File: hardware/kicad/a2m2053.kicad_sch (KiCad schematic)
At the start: 0 parts

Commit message: feat(pcb): frame-ground mounting holes H1/H2
Both M3 holes become plated footprints on net FG, placed from the
schematic. H2 uses the stock MountingHole_3.2mm_M3_Pad_Via. H1 sits
3.1 mm from the board edge, so it gets a project footprint with a
5.2 mm pad to keep 0.5 mm copper-to-edge. DRC: 0 violations; the
only unconnected item is FG between H1 and H2, not routed yet.

The outline script no longer draws hole circles; it positions H1/H2,
with a warning that footprint moves through the API crashed KiCad.

Co-Authored-By: Claude Opus 5.5 <noreply@anthropic.com>
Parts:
- added H1: M3 frame ground, a2m2053:MountingHole_3.2mm_M3_Pad_5.2mm, symbol Mechanical:MountingHole_Pad
- added H2: M3 frame ground, MountingHole:MountingHole_3.2mm_M3_Pad_Via, symbol Mechanical:MountingHole_Pad
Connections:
- new net FG: H1.1, H2.1
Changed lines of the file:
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@@
 	(generator_version "9.0")
 	(paper "A4")
+	(symbol
+		(lib_id "Mechanical:MountingHole_Pad")
+		(at 101.6 50.8 0)
+		(unit 1)
+		(exclude_from_sim no)
+		(in_bom no)
+		(on_board yes)
+		(dnp no)
+		(property "Reference" "H1"
+			(at 104.14 46.989999999999995 0)
+			(effects (font (size 1.27 1.27)) (justify left))
+		)
+		(property "Value" "M3 frame ground"
+			(at 104.14 49.529999999999994 0)
+			(effects (font (size 1.27 1.27)) (justify left))
+		)
+		(property "Footprint" "a2m2053:MountingHole_3.2mm_M3_Pad_5.2mm"
+			(at 101.6 50.8 0)
+			(effects (font (size 1.27 1.27)) (hide yes))
+		)
+		(property "Datasheet" "~"
+			(at 101.6 50.8 0)
+			(effects (font (size 1.27 1.27)) (hide yes))
+		)
+		(property "Description" "Mounting hole to the chassis, frame ground"
+			(at 101.6 50.8 0)
+			(effects (font (size 1.27 1.27)) (hide yes))
+		)
+		(pin "1"
+		)
+		(instances
+			(project "a2m2053"
+				(path "/a667a28b-9b2a-40ce-b2bb-952e798c6355"
+					(reference "H1")
+					(unit 1)
+				)
+			)
+		)
+	)
+	(global_label "FG"
+		(shape passive)
+		(at 101.6 53.34 270)
+		(effects (font (size 1.27 1.27)) (justify right))
+		(property "Intersheetrefs" "${INTERSHEET_REFS}"
+			(at 0 0 0)
+			(effects (font (size 1.27 1.27)) (hide yes))
+		)
+	)
+	(symbol
+		(lib_id "Mechanical:MountingHole_Pad")
+		(at 121.92 50.8 0)
+		(unit 1)
+		(exclude_from_sim no)
+		(in_bom no)
+		(on_board yes)
+		(dnp no)
+		(property "Reference" "H2"
+			(at 124.46000000000001 46.989999999999995 0)
+			(effects (font (size 1.27 1.27)) (justify left))
+		)
+		(property "Value" "M3 frame ground"
+			(at 124.46000000000001 49.529999999999994 0)
+			(effects (font (size 1.27 1.27)) (justify left))
+		)
+		(property "Footprint" "MountingHole:MountingHole_3.2mm_M3_Pad_Via"
+			(at 121.92 50.8 0)
+			(effects (font (size 1.27 1.27)) (hide yes))
+		)
+		(property "Datasheet" "~"
+			(at 121.92 50.8 0)
+			(effects (font (size 1.27 1.27)) (hide yes))
+		)
+		(property "Description" "Mounting hole to the chassis, frame ground"
+			(at 121.92 50.8 0)
+			(effects (font (size 1.27 1.27)) (hide yes))
+		)
+		(pin "1"
+		)
+		(instances
+			(project "a2m2053"
+				(path "/a667a28b-9b2a-40ce-b2bb-952e798c6355"
+					(reference "H2")
+					(unit 1)
+				)
+			)
+		)
+	)
+	(global_label "FG"
+		(shape passive)
+		(at 121.92 53.34 270)
+		(effects (font (size 1.27 1.27)) (justify right))
+		(property "Intersheetrefs" "${INTERSHEET_REFS}"
+			(at 0 0 0)
+			(effects (font (size 1.27 1.27)) (hide yes))
+		)
+	)
 	(sheet_instances
 		(path "/"

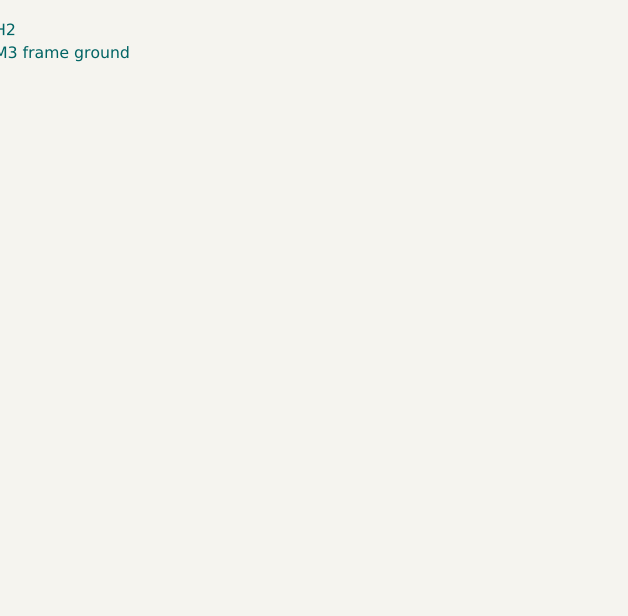
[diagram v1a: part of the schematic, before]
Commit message: feat(pcb): rear DB-19 J1 placed and fit-checked, step depths corrected
- J1: female right-angle DB-19 (daisy-chain port), 38.8 mm board-lock
  footprint on FG, face at the 94 mm top edge. Placement checked with a
  3D print holding the real connector on the IF-83 mounting points and
  in the case opening.
- Outline steps are 12 mm deep on the left and 6 mm on the right, checked
  on the IF-83. kicad_outline.py gains --outline-only.
- Photos of the fit check, EXIF stripped.

Co-Authored-By: Claude Opus 5.5 <noreply@anthropic.com>
Claude-Session: https://claude.ai/code/session_019cEGosXJSu4icn9o4uaZwB
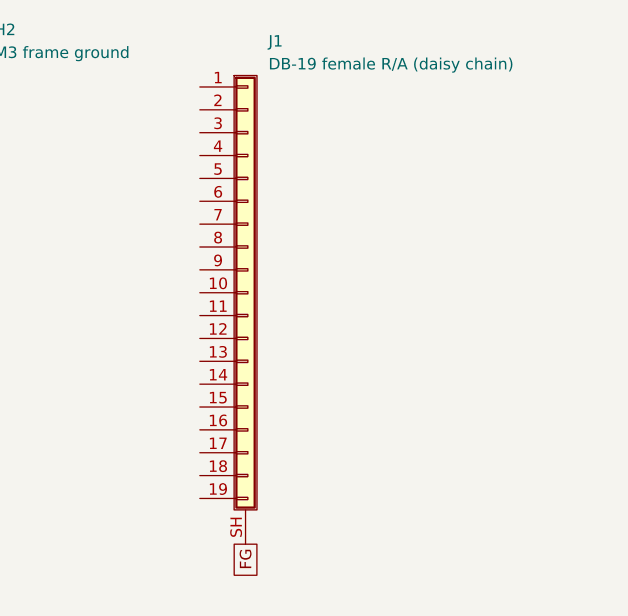
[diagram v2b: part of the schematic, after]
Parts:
- added J1: DB-19 female R/A (daisy chain), a2m2053:DSUB-19_Female_Horizontal_P2.77x2.84mm_MountingHoles38.8mm, symbol Connector_Generic_Shielded:Conn_01x19_Shielded
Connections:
- net FG: now also J1.SH (Shield)
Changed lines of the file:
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@@
+		)
+	)
+	(symbol
+		(lib_id "Connector_Generic_Shielded:Conn_01x19_Shielded")
+		(at 152.4 76.2 0)
+		(unit 1)
+		(exclude_from_sim no)
+		(in_bom yes)
+		(on_board yes)
+		(dnp no)
+		(property "Reference" "J1"
+			(at 154.94 48.260000000000005 0)
+			(effects (font (size 1.27 1.27)) (justify left))
+		)
+		(property "Value" "DB-19 female R/A (daisy chain)"
+			(at 154.94 50.800000000000004 0)
+			(effects (font (size 1.27 1.27)) (justify left))
+		)
+		(property "Footprint" "a2m2053:DSUB-19_Female_Horizontal_P2.77x2.84mm_MountingHoles38.8mm"
+			(at 152.4 76.2 0)
+			(effects (font (size 1.27 1.27)) (hide yes))
+		)
+		(property "Datasheet" "~"
+			(at 152.4 76.2 0)
+			(effects (font (size 1.27 1.27)) (hide yes))
+		)
+		(property "Description" "Rear DB-19 daisy-chain port, female right angle; shell board locks on FG"
+			(at 152.4 76.2 0)
+			(effects (font (size 1.27 1.27)) (hide yes))
+		)
+		(pin "1"
+		)
+		(pin "2"
+		)
+		(pin "3"
+		)
+		(pin "4"
+		)
+		(pin "5"
+		)
+		(pin "6"
+		)
+		(pin "7"
+		)
+		(pin "8"
+		)
+		(pin "9"
+		)
+		(pin "10"
+		)
+		(pin "11"
+		)
+		(pin "12"
+		)
+		(pin "13"
+		)
+		(pin "14"
+		)
+		(pin "15"
+		)
+		(pin "16"
+		)
+		(pin "17"
+		)
+		(pin "18"
+		)
+		(pin "19"
+		)
+		(pin "SH"
+		)
+		(instances
+			(project "a2m2053"
+				(path "/a667a28b-9b2a-40ce-b2bb-952e798c6355"
+					(reference "J1")
+					(unit 1)
+				)
+			)
+		)
+	)
+	(global_label "FG"
+		(shape passive)
+		(at 152.4 104.14 270)
+		(effects (font (size 1.27 1.27)) (justify right))
+		(property "Intersheetrefs" "${INTERSHEET_REFS}"
+			(at 0 0 0)
+			(effects (font (size 1.27 1.27)) (hide yes))
 		)
 	)

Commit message: feat(pcb): schematic wired, parts placed, board autorouted
Schematic: Pico 2 (A1), five SN74LVC8T245 (U1-U5) with one 100 nF per
rail, pull-ups/pull-downs, D1 Schottky to VSYS, 4.7 uF 50 V bulk caps,
J2 (CN104) and J3 (CN102) 2x10 headers, J4 eject and J5 LED headers.

Board: all parts placed inside the IF-83 outline, Pico USB at the bottom
edge. Netclasses Power (+5V, +12V, -12V: 1.0 mm), Rail (+3V3, VSYS:
0.5 mm). GND pour on B.Cu, +5V pour on F.Cu. Tracks from Freerouting
2.1.0 (r5, 80 vias); -12V J1.5 to J3.9 routed by hand at 0.25 mm.

Routing scratch (DSN/SES runs, DRC dumps, helper scripts) lives in
hardware/kicad/scratch/, git-ignored except for its .gitkeep.

DRC: 0 unconnected. Open: EJECT via 0.42 mm from the left edge, starved
thermals on J1.4 and J3.5, silkscreen warnings, A1 library mismatch.

Co-Authored-By: Claude Opus 5.5 <noreply@anthropic.com>
Claude-Session: https://claude.ai/code/session_019cEGosXJSu4icn9o4uaZwB
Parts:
- added A1: Pico 2, Module:RaspberryPi_Pico_SMD_HandSolder, symbol MCU_Module:RaspberryPi_Pico
- added C1, C10, C2, C3, C4, C5, C6, C7, C8, C9: 100nF, Capacitor_SMD:C_0805_2012Metric, symbol Device:C
- added C11, C12, C13: 4.7uF 50V, Capacitor_THT:CP_Radial_D5.0mm_P2.00mm, symbol Device:C_Polarized
- added D1: STPS2L40AF, Diode_SMD:D_SMA, symbol Device:D_Schottky_Small
- added J2: CN104 mechanism, Connector_IDC:IDC-Header_2x10_P2.54mm_Vertical, symbol Connector_Generic:Conn_02x10_Odd_Even
- added J3: CN102 host (FROM HOST), Connector_IDC:IDC-Header_2x10_P2.54mm_Vertical, symbol Connector_Generic:Conn_02x10_Odd_Even
- added J4: Eject button, Connector_PinHeader_2.54mm:PinHeader_1x03_P2.54mm_Vertical, symbol Connector_Generic:Conn_01x03
- added J5: In-use LED, Connector_PinHeader_2.54mm:PinHeader_1x02_P2.54mm_Vertical, symbol Connector_Generic:Conn_01x02
- added R1, R11, R12, R13, R14, R15, R2, R3, R4, R5, R6, R7, R8, R9: 10k, Resistor_SMD:R_1206_3216Metric, symbol Device:R
- added R10: 100k, Resistor_SMD:R_1206_3216Metric, symbol Device:R
- added R16: 2k, Resistor_SMD:R_1206_3216Metric, symbol Device:R
- added R17: 330, Resistor_SMD:R_1206_3216Metric, symbol Device:R
- added U1, U2, U3, U4, U5: SN74LVC8T245DWR, Package_SO:SOIC-24W_7.5x15.4mm_P1.27mm, symbol Logic_LevelTranslator:SN74LVC8T245
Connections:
- net GND: now reaches J1.1 (Pin_1)
- net GND: now also J1.2 (Pin_2), J1.3 (Pin_3), J1.4 (Pin_4), A1.13 (GND), A1.18 (GND), A1.23 (GND), A1.28 (GND), A1.3 (GND), A1.33 (AGND), A1.38 (GND), A1.8 (GND), C1.2, C10.2, C11.2, C12.2, C13.2, C2.2, C3.2, C4.2, C5.2, C6.2, C7.2, C8.2, C9.2, J2.1 (Pin_1), J2.3 (Pin_3), J2.5 (Pin_5), J2.7 (Pin_7), J3.1 (Pin_1), J3.12 (Pin_12), J3.3 (Pin_3), J3.5 (Pin_5), J3.7 (Pin_7), J4.1 (Pin_1), J4.3 (Pin_3), J5.2 (Pin_2), R10.2, R14.2, R4.2, R5.2, R6.2, R7.2, U1.11 (GND), U1.12 (GND), U1.13 (GND), U1.2 (DIR), U1.22 (~{OE}), U2.11 (GND), U2.12 (GND), U2.13 (GND), U3.10 (A8), U3.11 (GND), U3.12 (GND), U3.13 (GND), U3.5 (A3), U3.6 (A4), U3.7 (A5), U3.8 (A6), U3.9 (A7), U4.10 (A8), U4.11 (GND), U4.12 (GND), U4.13 (GND), U4.6 (A4), U4.7 (A5), U4.8 (A6), U4.9 (A7), U5.11 (GND), U5.12 (GND), U5.13 (GND), U5.14 (B8), U5.15 (B7), U5.16 (B6), U5.17 (B5), U5.18 (B4), U5.19 (B3), U5.2 (DIR), U5.20 (B2), U5.22 (~{OE})
- net HOST_ACK: now reaches J1.10 (Pin_10)
- net HOST_ACK: now also J3.20 (Pin_20), R11.1, U3.20 (B2)
- net HOST_PH0: now reaches J1.11 (Pin_11)
- net HOST_PH0: now also J3.2 (Pin_2), R4.1, U1.21 (B1)
- net HOST_PH1: now reaches J1.12 (Pin_12)
- net HOST_PH1: now also J3.4 (Pin_4), R5.1, U1.20 (B2)
- net HOST_PH2: now reaches J1.13 (Pin_13)
- net HOST_PH2: now also J3.6 (Pin_6), R6.1, U1.19 (B3)
- net PH3_OUT: now reaches J1.14 (Pin_14)
- net PH3_OUT: now also R14.1, U4.21 (B1)
- net HOST_WRREQ: now reaches J1.15 (Pin_15)
- net HOST_WRREQ: now also J3.10 (Pin_10), R8.1, U1.17 (B5)
- net LASTONE: now reaches J1.16 (Pin_16)
- net LASTONE: now also R16.1, U5.21 (B1)
- net ENBL_OUT: now reaches J1.17 (Pin_17)
- net ENBL_OUT: now also R15.1, U4.20 (B2)
- net HOST_RD: now reaches J1.18 (Pin_18)
- net HOST_RD: now also J3.16 (Pin_16), U3.21 (B1)
- net HOST_WR: now reaches J1.19 (Pin_19)
- net HOST_WR: now also J3.18 (Pin_18), R10.1, U1.15 (B7)
- net -12V: now reaches J1.5 (Pin_5)
- net -12V: now also J3.9 (Pin_9)
- net +5V: now reaches J1.6 (Pin_6)
- net +5V: now also C10.1, C12.1, C2.1, C4.1, C6.1, C8.1, D1.2 (A), J2.11 (Pin_11), J2.20 (Pin_20), J3.11 (Pin_11), R1.2, R11.2, R15.2, R16.2, R2.2, R3.2, R8.2, R9.2, U1.23 (V_{CCB}), U1.24 (V_{CCB}), U2.23 (V_{CCB}), U2.24 (V_{CCB}), U3.23 (V_{CCB}), U3.24 (V_{CCB}), U4.23 (V_{CCB}), U4.24 (V_{CCB}), U5.23 (V_{CCB}), U5.24 (V_{CCB})
- net +12V: now reaches J1.7 (Pin_7)
- net +12V: now also J1.8 (Pin_8), C11.1, J2.13 (Pin_13), J2.15 (Pin_15), J2.17 (Pin_17), J2.19 (Pin_19), J3.13 (Pin_13), J3.15 (Pin_15)
- net HDSEL: now reaches J1.9 (Pin_9)
- net HDSEL: now also J3.17 (Pin_17)
- new net +3V3: A1.36 (3V3), C1.1, C13.1, C3.1, C5.1, C7.1, C9.1, R12.2, R13.2, U1.1 (V_{CCA}), U2.1 (V_{CCA}), U2.2 (DIR), U3.1 (V_{CCA}), U3.2 (DIR), U4.1 (V_{CCA}), U4.2 (DIR), U5.1 (V_{CCA})
- new net ACK_A: A1.12 (GPIO9), U3.4 (A2)
- new net CA0_A: A1.16 (GPIO12), U2.3 (A1)
- new net CA1_A: A1.17 (GPIO13), U2.4 (A2)
- new net CA2_A: A1.19 (GPIO14), U2.5 (A3)
- new net EJECT: A1.29 (GPIO22), J4.2 (Pin_2)
- new net ENBL_A: A1.22 (GPIO17), U2.8 (A6)
- new net ENBL_OUT_A: A1.32 (GPIO27_ADC1), U4.4 (A2)
- new net HOST_HSTEN: J3.14 (Pin_14), R9.1, U1.16 (B6)
- new net HOST_PH3: J3.8 (Pin_8), R7.1, U1.18 (B4)
- new net HOST_RD_A: A1.14 (GPIO10), U3.3 (A1)
- new net HSTEN_A: A1.10 (GPIO7), U1.8 (A6)
- new net LASTONE_A: A1.2 (GPIO1), U5.3 (A1)
- new net LED: J5.1 (Pin_1), R17.2
- new net LED_A: A1.31 (GPIO26_ADC0), U4.5 (A3)
- new net LED_B: R17.1, U4.19 (B3)
- new net LSTRB_A: A1.20 (GPIO15), U2.6 (A4)
- new net MECH_CA0: J2.2 (Pin_2), U2.21 (B1)
- new net MECH_CA1: J2.4 (Pin_4), U2.20 (B2)
- new net MECH_CA2: J2.6 (Pin_6), U2.19 (B3)
- new net MECH_ENBL: J2.14 (Pin_14), R2.1, U2.16 (B6)
- new net MECH_LSTRB: J2.8 (Pin_8), U2.18 (B4)
- new net MECH_RD: J2.16 (Pin_16), R1.1, U1.14 (B8)
- new net MECH_RD_A: A1.26 (GPIO20), U1.10 (A8)
- new net MECH_SEL: J2.12 (Pin_12), U2.17 (B5)
- new net MECH_WRTDATA: J2.18 (Pin_18), U2.14 (B8)
- new net MECH_WRTGATE: J2.10 (Pin_10), R3.1, U2.15 (B7)
- new net PH0_A: A1.4 (GPIO2), U1.3 (A1)
- new net PH1_A: A1.5 (GPIO3), U1.4 (A2)
- new net PH2_A: A1.6 (GPIO4), U1.5 (A3)
- new net PH3_A: A1.7 (GPIO5), U1.6 (A4)
- new net PH3_OUT_A: A1.1 (GPIO0), U4.3 (A1)
- new net SEL_A: A1.21 (GPIO16), U2.7 (A5)
- new net U2_OE: A1.27 (GPIO21), R13.1, U2.22 (~{OE}), U4.22 (~{OE})
- new net U3_OE: A1.15 (GPIO11), R12.1, U3.22 (~{OE})
- new net VSYS: A1.39 (VSYS), D1.1 (K)
- new net WRREQ_A: A1.9 (GPIO6), U1.7 (A5)
- new net WRTDATA_A: A1.25 (GPIO19), U2.10 (A8)
- new net WRTGATE_A: A1.24 (GPIO18), U2.9 (A7)
- new net WR_A: A1.11 (GPIO8), U1.9 (A7)
- no-connect marks 0 -> 25
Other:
- moved on the sheet: J1

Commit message: feat(pcb): place and route the controller board
Schematic: add R18 (10k LSTRB pull-down to GND, matches the rig) and
re-order 8T245 channels on U1, U2 and U5 so the fan-outs do not cross.
HANDOFF lists the eight prototype rewires.

PCB: place all parts, route host, rear, mechanism and Pico fan-outs,
+5V and GND pours, a +12V band under the mechanism power path, stitch
the Pico GND castellations and the host pull-up pour strips. DRC with
zone refill: 0 errors; one stray via to delete in pcbnew (noted in
HANDOFF).

Co-Authored-By: Claude Fable 5.1 <noreply@anthropic.com>
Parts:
- added R18: 10k, Resistor_SMD:R_1206_3216Metric, symbol Device:R
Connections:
- net CA0_A: now also U2.6 (A4); no longer U2.3 (A1)
- net CA1_A: now also U2.5 (A3); no longer U2.4 (A2)
- net CA2_A: now also U2.4 (A2); no longer U2.5 (A3)
- net GND: now also R18.2
- net HOST_HSTEN: now also U1.15 (B7); no longer U1.16 (B6)
- net HOST_WR: now also U1.14 (B8); no longer U1.15 (B7)
- net HSTEN_A: now also U1.9 (A7); no longer U1.8 (A6)
- net LASTONE: now also U1.16 (B6); no longer U5.21 (B1)
- net LASTONE_A: now also U1.8 (A6); no longer U5.3 (A1)
- net LSTRB_A: now also U2.3 (A1); no longer U2.6 (A4)
- net MECH_CA0: now also U2.18 (B4); no longer U2.21 (B1)
- net MECH_CA1: now also U2.19 (B3); no longer U2.20 (B2)
- net MECH_CA2: now also U2.20 (B2); no longer U2.19 (B3)
- net MECH_LSTRB: now also U2.21 (B1), R18.1; no longer U2.18 (B4)
- net MECH_RD: now also U5.21 (B1); no longer U1.14 (B8)
- net MECH_RD_A: now also U5.3 (A1); no longer U1.10 (A8)
- net WR_A: now also U1.10 (A8); no longer U1.9 (A7)

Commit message: feat(pcb): Byte Hamr logo and board text, FG merged into GND
Silkscreen: logo_sm footprint from Byte Hamr rev 2 (copied into the
project library), title, revision and ID block in the bottom-right
corner. Board named Disk Hamr.

Schematic: the three FG global labels on H1, H2 and the J1 shield become
GND power symbols; FG was a fit-test placeholder, frame ground is the
same return. PCB pads were already on GND. Schematic parity, DRC with
refill and ERC are clean apart from the pre-existing Pico AGND/GND pin
type error.

Co-Authored-By: Claude Fable 5.1 <noreply@anthropic.com>
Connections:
- net FG is gone; now on net GND: H1.1, H2.1, J1.SH (Shield)
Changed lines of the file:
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@@
 		)
 	)
-	(global_label "FG"
-		(shape passive)
-		(at 370.84 130.81 270)
-		(effects
-			(font
-				(size 1.27 1.27)
-			)
-			(justify right)
-		)
-		(property "Intersheetrefs" "${INTERSHEET_REFS}"
-			(at 370.84 130.81 0)
-			(hide yes)
-			(show_name no)
-			(do_not_autoplace no)
-			(effects
-				(font
-					(size 1.27 1.27)
-				)
-			)
-		)
-	)
-	(global_label "FG"
-		(shape passive)
-		(at 101.6 53.34 270)
-		(effects
-			(font
-				(size 1.27 1.27)
-			)
-			(justify right)
-		)
-		(property "Intersheetrefs" "${INTERSHEET_REFS}"
-			(at 101.6 57.5725 90)
-			(hide yes)
-			(show_name no)
-			(do_not_autoplace no)
-			(effects
-				(font
-					(size 1.27 1.27)
-				)
-				(justify right)
-			)
-		)
-	)
-	(global_label "FG"
-		(shape passive)
-		(at 121.92 53.34 270)
-		(effects
-			(font
-				(size 1.27 1.27)
-			)
-			(justify right)
-		)
-		(property "Intersheetrefs" "${INTERSHEET_REFS}"
-			(at 121.92 57.5725 90)
-			(hide yes)
-			(show_name no)
-			(do_not_autoplace no)
-			(effects
-				(font
-					(size 1.27 1.27)
-				)
-				(justify right)
-			)
-		)
-	)
 	(symbol
 		(lib_id "Connector_Generic:Conn_02x10_Odd_Even")
@@
 					(unit 1)
 				)
+			)
+		)
+	)
+	(symbol
+		(lib_id "power:GND")
+		(at 370.84 130.81 0)
+		(unit 1)
+		(in_bom yes)
+		(on_board yes)
+		(dnp no)
+		(property "Reference" "#PWR010"
+			(at 370.84 137.16 0)
+			(hide yes)
+			(effects
+				(font
+					(size 1.27 1.27)
+				)
+			)
+		)
+		(property "Value" "GND"
+			(at 370.84 134.62 0)
+			(effects
+				(font
+					(size 1.27 1.27)
+				)
+			)
+		)
+		(property "Footprint" ""
+			(at 370.84 130.81 0)
+			(hide yes)
+			(effects
+				(font
+					(size 1.27 1.27)
+				)
+			)
+		)
+		(property "Datasheet" ""
+			(at 370.84 130.81 0)
+			(hide yes)
+			(effects
+				(font
+					(size 1.27 1.27)
+				)
+			)
+		)
+		(property "Description" "Power symbol creates a global label with name \"GND\" , ground"
+			(at 370.84 130.81 0)
+			(hide yes)
+			(effects
+				(font
+					(size 1.27 1.27)
+				)
+			)
+		)
+		(instances
+			(project "a2m2053"
+				(path "/a667a28b-9b2a-40ce-b2bb-952e798c6355"
+					(reference "#PWR010")
+					(unit 1)
+				)
+			)
+		)
+	)
+	(symbol
+		(lib_id "power:GND")
+		(at 101.6 53.34 0)
+		(unit 1)
+		(in_bom yes)
+		(on_board yes)
+		(dnp no)
+		(property "Reference" "#PWR011"
+			(at 101.6 59.69 0)
+			(hide yes)
+			(effects
+				(font
+					(size 1.27 1.27)
+				)
+			)
+		)
+		(property "Value" "GND"
+			(at 101.6 57.15 0)
+			(effects
+				(font
+					(size 1.27 1.27)
+				)
+			)
+		)
+		(property "Footprint" ""
+			(at 101.6 53.34 0)
+			(hide yes)
+			(effects
+				(font
+					(size 1.27 1.27)
+				)
+			)
+		)
+		(property "Datasheet" ""
+			(at 101.6 53.34 0)
+			(hide yes)
+			(effects
+				(font
+					(size 1.27 1.27)
+				)
+			)
+		)
+		(property "Description" "Power symbol creates a global label with name \"GND\" , ground"
+			(at 101.6 53.34 0)
+			(hide yes)
+			(effects
+				(font
+					(size 1.27 1.27)
+				)
+			)
+		)
+		(instances
+			(project "a2m2053"
+				(path "/a667a28b-9b2a-40ce-b2bb-952e798c6355"
+					(reference "#PWR011")
+					(unit 1)
+				)
+			)
+		)
+	)
+	(symbol
+		(lib_id "power:GND")
+		(at 121.92 53.34 0)
+		(unit 1)
+		(in_bom yes)
+		(on_board yes)
+		(dnp no)
+		(property "Reference" "#PWR012"
+			(at 121.92 59.69 0)
+			(hide yes)
+			(effects
+				(font
+					(size 1.27 1.27)
+				)
+			)
+		)
+		(property "Value" "GND"
+			(at 121.92 57.15 0)
+			(effects
+				(font
+					(size 1.27 1.27)
+				)
+			)
+		)
+		(property "Footprint" ""
+			(at 121.92 53.34 0)
+			(hide yes)
+			(effects
+				(font
+					(size 1.27 1.27)
+				)
+			)
+		)
+		(property "Datasheet" ""
+			(at 121.92 53.34 0)
+			(hide yes)
+			(effects
+				(font
+					(size 1.27 1.27)
+				)
+			)
+		)
+		(property "Description" "Power symbol creates a global label with name \"GND\" , ground"
+			(at 121.92 53.34 0)
+			(hide yes)
+			(effects
+				(font
+					(size 1.27 1.27)
+				)
+			)
+		)
+		(instances
+			(project "a2m2053"
+				(path "/a667a28b-9b2a-40ce-b2bb-952e798c6355"
+					(reference "#PWR012")
+					(unit 1)
+				)

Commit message: feat(pcb): second layout of Disk Hamr rev 1.0, hand placed, +5V as traces
The 3D print put the mechanism header (J2) 11 mm too far from the
board edge, so the board was placed again by hand and re-routed with
Freerouting, then fixed up by hand.

- Shifters next to the connectors they serve: U2/U5 by J2, U1/U3/U4
  under J1/J3, Pico along the left edge.
- +5V pour on F.Cu removed. +5V is a Power net class now (1 mm
  track, 1 mm via) and is routed as traces; the pour had split into
  eleven islands under the signal traces and Freerouting treats a
  plane as already connected.
- +12V zone moved to B.Cu. GND stays a B.Cu plane; a fenced GND pocket
  under J1 is bridged with a top-side jumper.
- J4 (eject, 3-pin) and J5 (LED, 2-pin) swapped to the IF-83's order,
  shroud open toward the board edge. New TE AMP CT 2.00 mm footprints
  with the vendor STEP models (models are local, see docs/SOURCES.md).
- Logo footprint G1 re-placed from the library with the board-only
  attribute so Update PCB from Schematic leaves it alone.
- DRC with zone refill: 0 errors, 0 unconnected. 768 segments,
  123 vias.
- Top and bottom renders in hardware/kicad/render/.
- .gitignore: vendor 3D models and Freerouting .rules files.

Co-Authored-By: Claude Fable 5.1 <noreply@anthropic.com>
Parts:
- J4: footprint Connector_PinHeader_2.54mm:PinHeader_1x03_P2.54mm_Vertical -> a2m2053:TE_AMP_CT_1x03_P2.00mm_Vertical; MPN (none) -> 292161-3; Manufacturer (none) -> TE Connectivity
- J5: footprint Connector_PinHeader_2.54mm:PinHeader_1x02_P2.54mm_Vertical -> a2m2053:TE_AMP_CT_1x02_P2.00mm_Vertical; MPN (none) -> 292161-2; Manufacturer (none) -> TE Connectivity

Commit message: fix(pcb): R17 is 180 ohm, the IF-83's LED anode pull-up
Measured the LED pull-up on the IF-83: 180 ohm to +5V. Our board drives
the LED the same way (U4 output through R17, cathode to GND), so R17
takes the same value for the same brightness. About 17 mA from 5 V,
inside the 8T245's 32 mA output rating.

- Schematic and board: R17 value 330 -> 180. Footprint unchanged, so
  the fabrication outputs are unaffected.
- bom.csv / bom.md: R17 = 180 (Yageo RC1206FR-07180RL, DigiKey
  311-180FRCT-ND); the "keep 220 and 470 on hand" note is gone and the
  open item on the R17 value is closed.
- FABRICATION.md and research_notes.md record the measurement,
  2026-10-25.

Co-Authored-By: Claude Fable 5.1 <noreply@anthropic.com>
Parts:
- R17: value 330 -> 180
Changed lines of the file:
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@@
 			)
 		)
-		(property "Value" "330"
+		(property "Value" "180"
 			(at 243.84 215.9 90)
 			(show_name no)
